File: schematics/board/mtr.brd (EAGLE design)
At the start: 16 x 13 mm, 6 parts

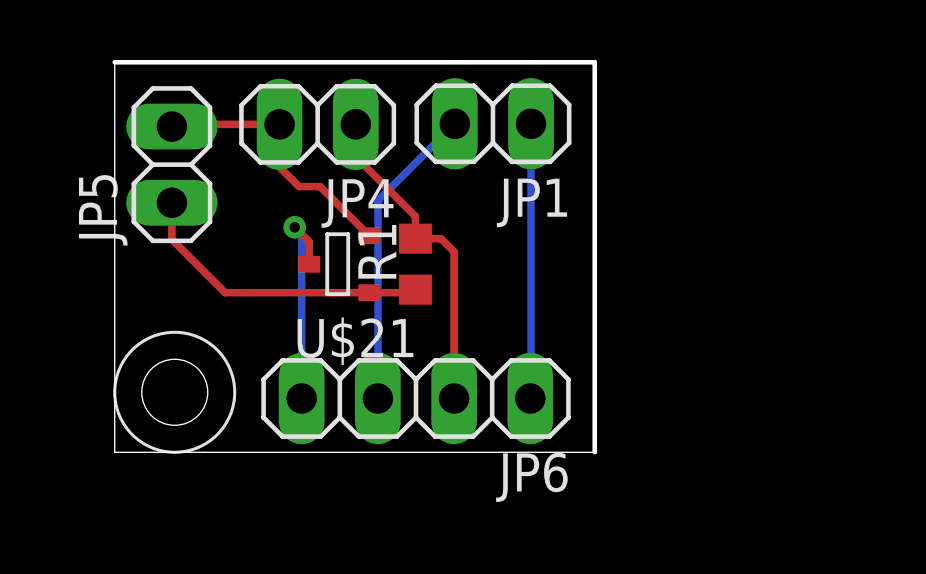
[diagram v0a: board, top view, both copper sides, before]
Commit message: Доделаны платы dop и mtr
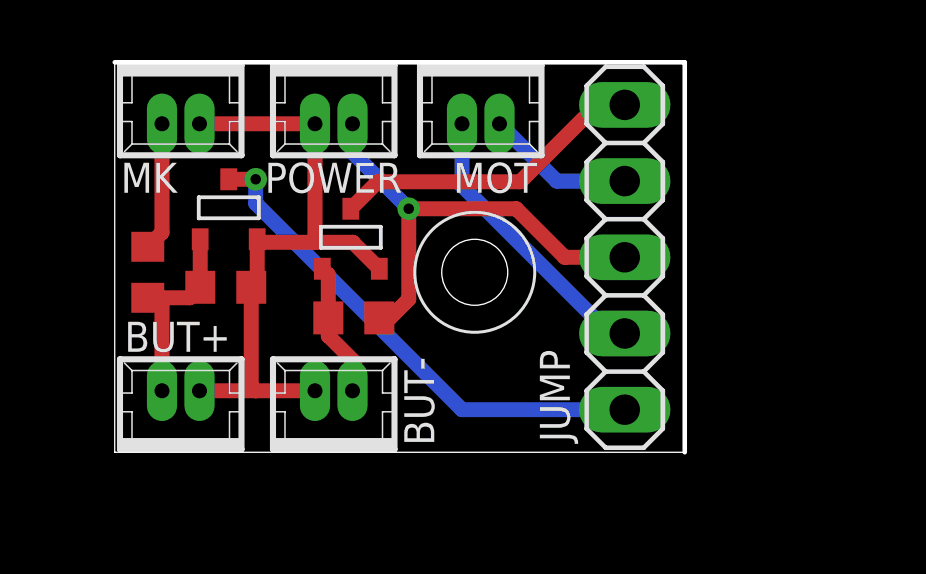
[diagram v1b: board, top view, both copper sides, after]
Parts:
- removed JP1, JP4, JP5: (no value), pinhead:1X02
- removed JP6: (no value), pinhead:1X04
- added BUT+, BUT-, MK, MOT, POWER: 53047-02, con-molex:53047-02
- added JUMP: (no value), pinhead:1X05
- added R11: 10k*2, rcl:R0603
- added R12: 1k, rcl:R0603
- added U$1: SI2302CDS, CanCubeSat:SOT23-3
- U$21: device CanCubeSat:SI2302CDS -> CanCubeSat:SOT23-3
- moved R1 2.73 mm to (7.97, 4.48), turned to 0 degrees
- moved U$21 0.93 mm to (7.87, 7.12), turned to 0 degrees
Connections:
- removed net MOTOR-G: JP6.4, U$21.3
- new net MOTOR3+G: JUMP.5, U$21.3
- new net MOTOR3-G: JUMP.1, U$1.3
- new net N$17: BUT+.2, R11.1, R12.2, U$1.1
- new net TRUBKI: MK.1, R12.1
- net 12V: now also JUMP.3, POWER.2; no longer JP4.1, JP6.2
- net GND: now also BUT+.1, BUT-.2, MK.2, POWER.1, R11.2, U$1.2; no longer JP4.2, JP5.2
- net MOTOR3+: now also JUMP.4, MOT.2; no longer JP1.2, JP6.3
- net MOTOR3-: now also JUMP.2, MOT.1; no longer JP1.1, JP6.1
- net N$1: now also BUT-.1; no longer JP5.1
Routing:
- net MOTOR3-G: track 0.00 -> 16.8 mm, vias 0 -> 1
- net GND: track 8.98 -> 21.3 mm
- net MOTOR3+G: track 0.00 -> 10.6 mm
- net MOTOR-G: track 7.23 -> 0.00 mm, vias 1 -> 0
- net N$17: track 0.00 -> 7.07 mm
- net N$1: track 10.1 -> 4.55 mm
- net MOTOR3+: track 10.2 -> 4.97 mm
- net 12V: track 11.0 -> 15.7 mm, vias 0 -> 1
- net TRUBKI: track 0.00 -> 4.30 mm
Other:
- board size 16 x 13 mm -> 19 x 13 mm

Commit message: Подготовлены платы SP и mtr
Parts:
- moved JUMP 6.00 mm to (23.0, 6.50)
- moved MOT 6.00 mm to (18.2, 11.4)
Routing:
- net 12V: track 15.7 -> 21.9 mm
- net MOTOR3-G: track 16.8 -> 22.8 mm
- net MOTOR3+G: track 10.6 -> 16.6 mm
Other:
- board size 19 x 13 mm -> 25 x 13 mm
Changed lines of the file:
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@@
 <board>
 <plain>
-<wire x1="0" y1="0" x2="19" y2="0" width="0" layer="20"/>
-<hole x="12" y="6" drill="2.2"/>
-<wire x1="0" y1="13" x2="0" y2="0" width="0" layer="20"/>
-<wire x1="0" y1="13" x2="19" y2="13" width="0.1524" layer="20"/>
-<wire x1="19" y1="13" x2="19" y2="0" width="0.1524" layer="20"/>
-<circle x="12" y="6" radius="2" width="0.1" layer="21"/>
+<wire x1="0" y1="0" x2="25" y2="0" width="0.1" layer="20"/>
+<hole x="12.5" y="6.5" drill="2.2"/>
+<wire x1="0" y1="13" x2="0" y2="0" width="0.1" layer="20"/>
+<wire x1="0" y1="13" x2="25" y2="13" width="0.1" layer="20"/>
+<wire x1="25" y1="13" x2="25" y2="0" width="0.1" layer="20"/>
+<circle x="12.5" y="6.5" radius="2" width="0.1" layer="21"/>
 </plain>
 <attributes>
@@
 </element>
 <element name="U$21" library="CanCubeSat" package="SOT23-3" value="SI2302CDS" x="7.869" y="7.117" smashed="yes"/>
-<element name="JUMP" library="pinhead" library_urn="urn:adsk.eagle:library:325" package="1X05" package3d_urn="urn:adsk.eagle:package:22469/2" value="" x="17" y="6.5" smashed="yes" rot="R90">
-<attribute name="NAME" x="15.1712" y="0.3438" size="1" layer="25" ratio="15" rot="R90"/>
-<attribute name="POPULARITY" value="69" x="17" y="6.5" size="1.778" layer="27" rot="R90" display="off"/>
-<attribute name="VALUE" x="20.175" y="1.42" size="1.27" layer="27" rot="R90"/>
+<element name="JUMP" library="pinhead" library_urn="urn:adsk.eagle:library:325" package="1X05" package3d_urn="urn:adsk.eagle:package:22469/2" value="" x="23" y="6.5" smashed="yes" rot="R90">
+<attribute name="NAME" x="21.1712" y="0.3438" size="1" layer="25" ratio="15" rot="R90"/>
+<attribute name="POPULARITY" value="69" x="23" y="6.5" size="1.778" layer="27" rot="R90" display="off"/>
+<attribute name="VALUE" x="26.175" y="1.42" size="1.27" layer="27" rot="R90"/>
 </element>
 <element name="U$1" library="CanCubeSat" package="SOT23-3" value="SI2302CDS" x="3.8" y="8.1" smashed="yes"/>
@@
 <attribute name="POPULARITY" value="0" x="2.2" y="11.4" size="1.778" layer="27" rot="R180" display="off"/>
 </element>
-<element name="MOT" library="con-molex" library_urn="urn:adsk.eagle:library:165" package="53047-02" package3d_urn="urn:adsk.eagle:package:8078511/1" value="53047-02" x="12.2" y="11.4" smashed="yes" rot="R180">
-<attribute name="MF" value="MOLEX" x="12.2" y="11.4" size="1.778" layer="27" rot="R180" display="off"/>
-<attribute name="MPN" value="53047-0210" x="12.2" y="11.4" size="1.778" layer="27" rot="R180" display="off"/>
-<attribute name="NAME" x="14.075" y="9.65" size="1" layer="25" ratio="15" rot="R180"/>
-<attribute name="OC_FARNELL" value="9733051" x="12.2" y="11.4" size="1.778" layer="27" rot="R180" display="off"/>
-<attribute name="OC_NEWARK" value="57H4701" x="12.2" y="11.4" size="1.778" layer="27" rot="R180" display="off"/>
-<attribute name="POPULARITY" value="0" x="12.2" y="11.4" size="1.778" layer="27" rot="R180" display="off"/>
+<element name="MOT" library="con-molex" library_urn="urn:adsk.eagle:library:165" package="53047-02" package3d_urn="urn:adsk.eagle:package:8078511/1" value="53047-02" x="18.2" y="11.4" smashed="yes" rot="R180">
+<attribute name="MF" value="MOLEX" x="18.2" y="11.4" size="1.778" layer="27" rot="R180" display="off"/>
+<attribute name="MPN" value="53047-0210" x="18.2" y="11.4" size="1.778" layer="27" rot="R180" display="off"/>
+<attribute name="NAME" x="20.075" y="9.65" size="1" layer="25" ratio="15" rot="R180"/>
+<attribute name="OC_FARNELL" value="9733051" x="18.2" y="11.4" size="1.778" layer="27" rot="R180" display="off"/>
+<attribute name="OC_NEWARK" value="57H4701" x="18.2" y="11.4" size="1.778" layer="27" rot="R180" display="off"/>
+<attribute name="POPULARITY" value="0" x="18.2" y="11.4" size="1.778" layer="27" rot="R180" display="off"/>
 </element>
 <element name="POWER" library="con-molex" library_urn="urn:adsk.eagle:library:165" package="53047-02" package3d_urn="urn:adsk.eagle:package:8078511/1" value="53047-02" x="7.3" y="11.4" smashed="yes" rot="R180">
@@
 <contactref element="U$21" pad="3"/>
 <contactref element="JUMP" pad="5"/>
-<wire x1="13.517" y1="9.017" x2="8.769" y2="9.017" width="0.5" layer="1"/>
-<wire x1="7.869" y1="8.117" x2="8.769" y2="9.017" width="0.5" layer="1"/>
-<wire x1="16.08" y1="11.58" x2="17" y2="11.58" width="0.5" layer="1"/>
-<wire x1="13.517" y1="9.017" x2="16.08" y2="11.58" width="0.5" layer="1"/>
+<wire x1="19.817" y1="9.317" x2="9.069" y2="9.317" width="0.5" layer="1"/>
+<wire x1="7.869" y1="8.117" x2="9.069" y2="9.317" width="0.5" layer="1"/>
+<wire x1="22.08" y1="11.58" x2="23" y2="11.58" width="0.5" layer="1"/>
+<wire x1="19.817" y1="9.317" x2="22.08" y2="11.58" width="0.5" layer="1"/>
 </signal>
 <signal name="12V">
@@
 <contactref element="JUMP" pad="3"/>
 <contactref element="POWER" pad="2"/>
-<wire x1="17" y1="6.5" x2="15" y2="6.5" width="0.5" layer="1"/>
-<wire x1="13.383" y1="8.117" x2="9.8" y2="8.117" width="0.5" layer="1"/>
-<wire x1="9.8" y1="8.117" x2="9.8" y2="5.1" width="0.5" layer="1"/>
-<wire x1="9.8" y1="5.1" x2="9.177" y2="4.477" width="0.5" layer="1"/>
+<wire x1="23" y1="6.5" x2="21" y2="6.5" width="0.5" layer="1"/>
+<wire x1="19.083" y1="8.417" x2="9.7" y2="8.417" width="0.5" layer="1"/>
+<wire x1="9.7" y1="8.417" x2="9.7" y2="5" width="0.5" layer="1"/>
+<wire x1="9.7" y1="5" x2="9.177" y2="4.477" width="0.5" layer="1"/>
 <wire x1="8.819" y1="4.477" x2="9.177" y2="4.477" width="0.5" layer="1"/>
-<wire x1="15" y1="6.5" x2="13.383" y2="8.117" width="0.5" layer="1"/>
-<wire x1="7.925" y1="10.95" x2="7.925" y2="9.992" width="0.5" layer="16"/>
-<wire x1="7.925" y1="9.992" x2="9.8" y2="8.117" width="0.5" layer="16"/>
-<via x="9.8" y="8.117" extent="1-16" drill="0.35"/>
+<wire x1="21" y1="6.5" x2="19.083" y2="8.417" width="0.5" layer="1"/>
+<wire x1="7.925" y1="10.95" x2="7.925" y2="10.192" width="0.5" layer="16"/>
+<wire x1="7.925" y1="10.192" x2="9.7" y2="8.417" width="0.5" layer="16"/>
+<via x="9.7" y="8.417" extent="1-16" drill="0.35"/>
 </signal>
 <signal name="MOTOR3+">
 <contactref element="JUMP" pad="4"/>
 <contactref element="MOT" pad="2"/>
-<wire x1="17" y1="9.04" x2="14.735" y2="9.04" width="0.5" layer="16"/>
-<wire x1="14.735" y1="9.04" x2="12.825" y2="10.95" width="0.5" layer="16"/>
+<wire x1="23" y1="9.04" x2="20.735" y2="9.04" width="0.5" layer="16"/>
+<wire x1="20.735" y1="9.04" x2="18.825" y2="10.95" width="0.5" layer="16"/>
 </signal>
 <signal name="MOTOR3-">
 <contactref element="JUMP" pad="2"/>
 <contactref element="MOT" pad="1"/>
-<wire x1="17" y1="3.96" x2="16.5" y2="3.96" width="0.5" layer="16"/>
-<wire x1="16.5" y1="3.96" x2="11.575" y2="8.885" width="0.5" layer="16"/>
-<wire x1="11.575" y1="8.885" x2="11.575" y2="10.95" width="0.5" layer="16"/>
+<wire x1="23" y1="3.96" x2="22.5" y2="3.96" width="0.5" layer="16"/>
+<wire x1="22.5" y1="3.96" x2="17.575" y2="8.885" width="0.5" layer="16"/>
+<wire x1="17.575" y1="8.885" x2="17.575" y2="10.95" width="0.5" layer="16"/>
 </signal>
 <signal name="N$17">
@@
 <wire x1="11.58" y1="1.42" x2="4.7" y2="8.3" width="0.5" layer="16"/>
 <wire x1="4.7" y1="9.1" x2="4.7" y2="8.3" width="0.5" layer="16"/>
-<wire x1="11.58" y1="1.42" x2="17" y2="1.42" width="0.5" layer="16"/>
+<wire x1="11.58" y1="1.42" x2="23" y2="1.42" width="0.5" layer="16"/>
 </signal>
 </signals>
